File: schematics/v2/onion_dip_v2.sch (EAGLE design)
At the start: 38 parts, among them IC2 DS2432P

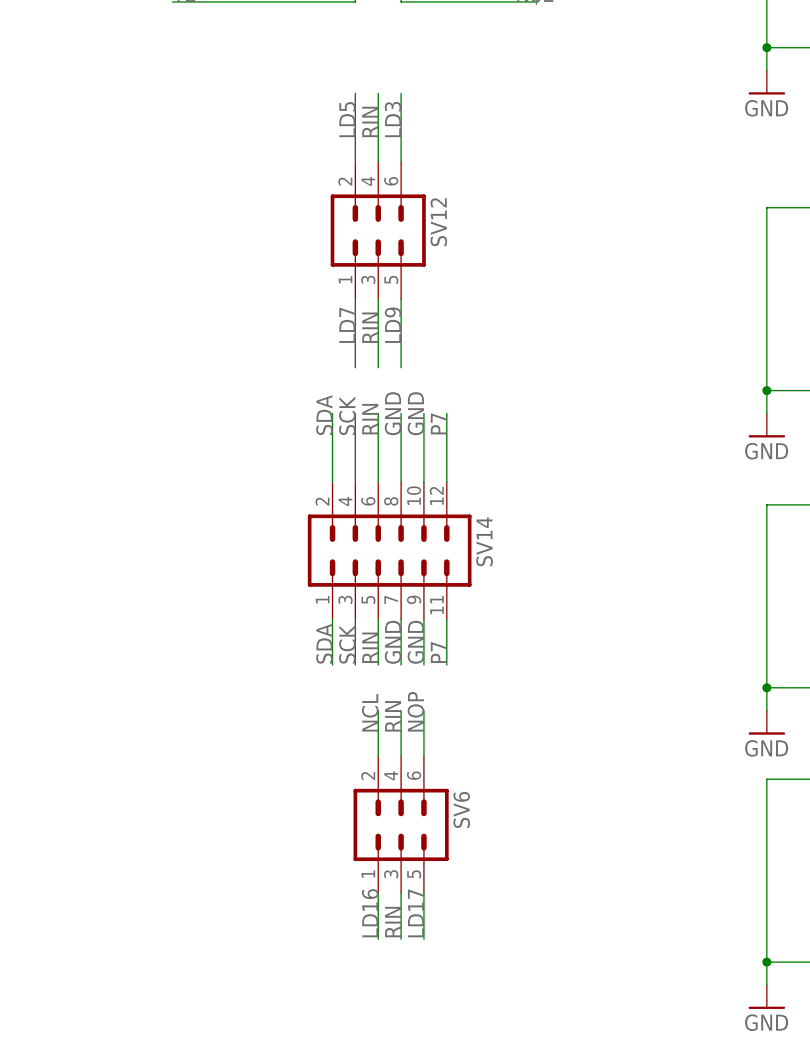
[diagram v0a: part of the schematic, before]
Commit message: increased isolation
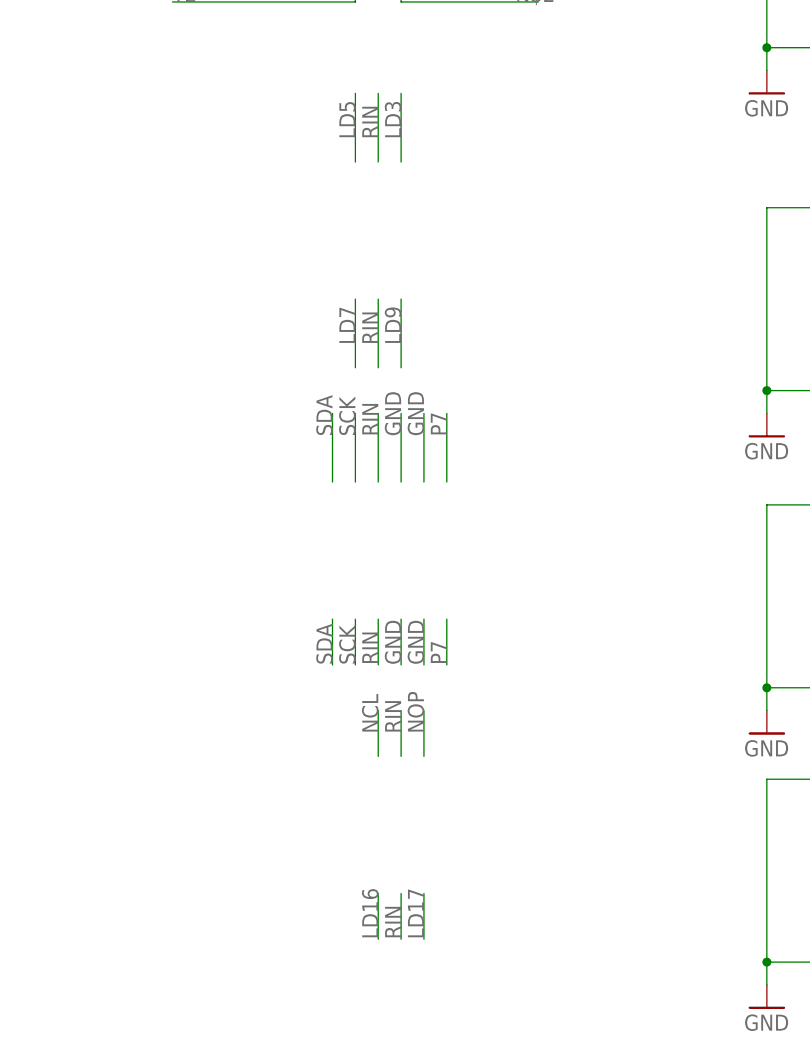
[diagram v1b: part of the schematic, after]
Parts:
- removed SV12, SV6: (no value), con-lstb_no_frame:MA03-2
- removed SV14: (no value), con-lstb_no_frame:MA06-2
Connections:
- net GND: no longer SV14.10, SV14.7, SV14.8, SV14.9
- net LD16: no longer SV6.1
- net LD17: no longer SV6.5
- net LD3: no longer SV12.6
- net LD5: no longer SV12.2
- net LD7: no longer SV12.1
- net LD9: no longer SV12.5
- net NCL: no longer SV6.2
- net NOP: no longer SV6.6
- net P7: no longer SV14.11, SV14.12
- net RIN: no longer SV12.3, SV12.4, SV14.5, SV14.6, SV6.3, SV6.4
- net SCK: no longer SV14.3, SV14.4
- net SDA: no longer SV14.1, SV14.2
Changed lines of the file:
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@@
 <part name="SV10" library="con-lstb_no_frame" deviceset="MA05-2" device=""/>
 <part name="SV11" library="con-lstb_no_frame" deviceset="MA05-2" device=""/>
-<part name="SV6" library="con-lstb_no_frame" deviceset="MA03-2" device=""/>
-<part name="SV12" library="con-lstb_no_frame" deviceset="MA03-2" device=""/>
-<part name="SV14" library="con-lstb_no_frame" deviceset="MA06-2" device=""/>
 <part name="SV20" library="con-lstb_no_frame" deviceset="MA07-2" device=""/>
 <part name="SV21" library="con-lstb_no_frame" deviceset="MA07-2" device=""/>
@@
 <instance part="SV10" gate="G$1" x="142.24" y="180.34" rot="R270"/>
 <instance part="SV11" gate="G$1" x="142.24" y="218.44" rot="R270"/>
-<instance part="SV6" gate="1" x="88.9" y="83.82" rot="R270"/>
-<instance part="SV12" gate="1" x="86.36" y="149.86" rot="R270"/>
-<instance part="SV14" gate="1" x="88.9" y="114.3" rot="R270"/>
 <instance part="SV20" gate="G$1" x="86.36" y="284.48" rot="R270"/>
 <instance part="SV21" gate="G$1" x="86.36" y="259.08" rot="R270"/>
@@
 </segment>
 <segment>
-<pinref part="SV14" gate="1" pin="2"/>
 <wire x1="81.28" y1="121.92" x2="81.28" y2="129.54" width="0.1524" layer="91"/>
 <label x="81.28" y="127" size="1.778" layer="95" rot="R90"/>
 </segment>
 <segment>
-<pinref part="SV14" gate="1" pin="1"/>
 <wire x1="81.28" y1="106.68" x2="81.28" y2="101.6" width="0.1524" layer="91"/>
 <label x="81.28" y="101.6" size="1.778" layer="95" rot="R90"/>
@@
 </segment>
 <segment>
-<pinref part="SV14" gate="1" pin="3"/>
 <wire x1="83.82" y1="106.68" x2="83.82" y2="101.6" width="0.1524" layer="91"/>
 <label x="83.82" y="101.6" size="1.778" layer="95" rot="R90"/>
 </segment>
 <segment>
-<pinref part="SV14" gate="1" pin="4"/>
 <wire x1="83.82" y1="121.92" x2="83.82" y2="129.54" width="0.1524" layer="91"/>
 <label x="83.82" y="127" size="1.778" layer="95" rot="R90"/>
@@
 </segment>
 <segment>
-<pinref part="SV14" gate="1" pin="8"/>
 <wire x1="88.9" y1="121.92" x2="88.9" y2="129.54" width="0.1524" layer="91"/>
 <label x="88.9" y="127" size="1.778" layer="95" rot="R90"/>
 </segment>
 <segment>
-<pinref part="SV14" gate="1" pin="10"/>
 <wire x1="91.44" y1="121.92" x2="91.44" y2="129.54" width="0.1524" layer="91"/>
 <label x="91.44" y="127" size="1.778" layer="95" rot="R90"/>
 </segment>
 <segment>
-<pinref part="SV14" gate="1" pin="7"/>
 <wire x1="88.9" y1="106.68" x2="88.9" y2="101.6" width="0.1524" layer="91"/>
 <label x="88.9" y="101.6" size="1.778" layer="95" rot="R90"/>
 </segment>
 <segment>
-<pinref part="SV14" gate="1" pin="9"/>
 <wire x1="91.44" y1="106.68" x2="91.44" y2="101.6" width="0.1524" layer="91"/>
 <label x="91.44" y="101.6" size="1.778" layer="95" rot="R90"/>
@@
 </segment>
 <segment>
-<pinref part="SV14" gate="1" pin="11"/>
 <wire x1="93.98" y1="106.68" x2="93.98" y2="101.6" width="0.1524" layer="91"/>
 <label x="93.98" y="101.6" size="1.778" layer="95" rot="R90"/>
 </segment>
 <segment>
-<pinref part="SV14" gate="1" pin="12"/>
 <wire x1="93.98" y1="121.92" x2="93.98" y2="129.54" width="0.1524" layer="91"/>
 <label x="93.98" y="127" size="1.778" layer="95" rot="R90"/>
@@
 </segment>
 <segment>
-<pinref part="SV6" gate="1" pin="1"/>
 <wire x1="86.36" y1="76.2" x2="86.36" y2="71.12" width="0.1524" layer="91"/>
 <label x="86.36" y="71.12" size="1.778" layer="95" rot="R90"/>
@@
 </segment>
 <segment>
-<pinref part="SV12" gate="1" pin="6"/>
 <wire x1="88.9" y1="157.48" x2="88.9" y2="165.1" width="0.1524" layer="91"/>
 <label x="88.9" y="160.02" size="1.778" layer="95" rot="R90"/>
@@
 </segment>
 <segment>
-<pinref part="SV12" gate="1" pin="2"/>
 <wire x1="83.82" y1="157.48" x2="83.82" y2="165.1" width="0.1524" layer="91"/>
 <label x="83.82" y="160.02" size="1.778" layer="95" rot="R90"/>
@@
 </segment>
 <segment>
-<pinref part="SV12" gate="1" pin="1"/>
 <wire x1="83.82" y1="142.24" x2="83.82" y2="134.62" width="0.1524" layer="91"/>
 <label x="83.82" y="137.16" size="1.778" layer="95" rot="R90"/>
@@
 </segment>
 <segment>
-<pinref part="SV12" gate="1" pin="5"/>
 <wire x1="88.9" y1="142.24" x2="88.9" y2="134.62" width="0.1524" layer="91"/>
 <label x="88.9" y="137.16" size="1.778" layer="95" rot="R90"/>
@@
 </segment>
 <segment>
-<pinref part="SV6" gate="1" pin="5"/>
 <wire x1="91.44" y1="76.2" x2="91.44" y2="71.12" width="0.1524" layer="91"/>
 <label x="91.44" y="71.12" size="1.778" layer="95" rot="R90"/>
@@
 </segment>
 <segment>
-<pinref part="SV12" gate="1" pin="3"/>
 <wire x1="86.36" y1="142.24" x2="86.36" y2="134.62" width="0.1524" layer="91"/>
 <label x="86.36" y="137.16" size="1.778" layer="95" rot="R90"/>
 </segment>
 <segment>
-<pinref part="SV14" gate="1" pin="6"/>
 <wire x1="86.36" y1="121.92" x2="86.36" y2="129.54" width="0.1524" layer="91"/>
 <label x="86.36" y="127" size="1.778" layer="95" rot="R90"/>
 </segment>
 <segment>
-<pinref part="SV14" gate="1" pin="5"/>
 <wire x1="86.36" y1="106.68" x2="86.36" y2="101.6" width="0.1524" layer="91"/>
 <label x="86.36" y="101.6" size="1.778" layer="95" rot="R90"/>
 </segment>
 <segment>
-<pinref part="SV6" gate="1" pin="4"/>
 <wire x1="88.9" y1="91.44" x2="88.9" y2="96.52" width="0.1524" layer="91"/>
 <label x="88.9" y="93.98" size="1.778" layer="95" rot="R90"/>
 </segment>
 <segment>
-<pinref part="SV6" gate="1" pin="3"/>
 <wire x1="88.9" y1="76.2" x2="88.9" y2="71.12" width="0.1524" layer="91"/>
 <label x="88.9" y="71.12" size="1.778" layer="95" rot="R90"/>
 </segment>
 <segment>
-<pinref part="SV12" gate="1" pin="4"/>
 <wire x1="86.36" y1="157.48" x2="86.36" y2="165.1" width="0.1524" layer="91"/>
 <label x="86.36" y="160.02" size="1.778" layer="95" rot="R90"/>
@@
 </segment>
 <segment>
-<pinref part="SV6" gate="1" pin="2"/>
 <wire x1="86.36" y1="91.44" x2="86.36" y2="96.52" width="0.1524" layer="91"/>
 <label x="86.36" y="93.98" size="1.778" layer="95" rot="R90"/>
@@
 </segment>
 <segment>
-<pinref part="SV6" gate="1" pin="6"/>
 <wire x1="91.44" y1="91.44" x2="91.44" y2="96.52" width="0.1524" layer="91"/>
 <label x="91.44" y="93.98" size="1.778" layer="95" rot="R90"/>

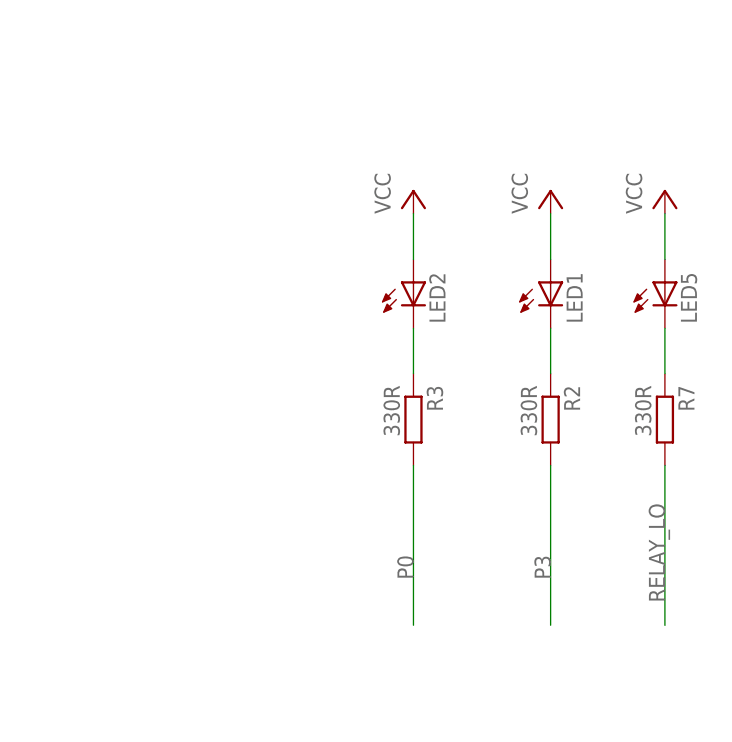
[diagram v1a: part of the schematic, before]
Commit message: changed led to 3.3V and reconnected LED1 to P1 (was P0)
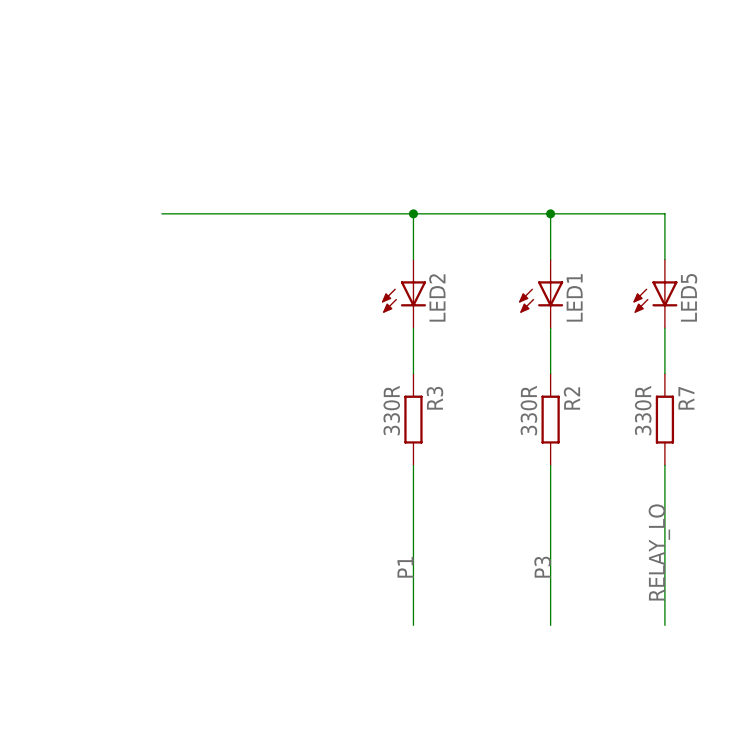
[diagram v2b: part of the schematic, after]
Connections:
- net P0: no longer R3.2
- net P1: now also R3.2
- net VCC: no longer LED1.A, LED2.A, LED5.A
- net _3V3: now also LED1.A, LED2.A, LED5.A
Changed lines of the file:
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@@
 <part name="SV20" library="con-lstb_no_frame" deviceset="MA07-2" device=""/>
 <part name="SV21" library="con-lstb_no_frame" deviceset="MA07-2" device=""/>
-<part name="P+2" library="supply1" deviceset="VCC" device=""/>
 <part name="P+4" library="supply1" deviceset="VCC" device=""/>
 <part name="P+6" library="supply1" deviceset="VCC" device=""/>
@@
 <part name="LED1" library="led" deviceset="LED" device="CHIP-LED0805"/>
 <part name="R2" library="rcl" deviceset="R-EU_" device="R0805" value="330R"/>
-<part name="P+5" library="supply1" deviceset="VCC" device=""/>
 <part name="LED2" library="led" deviceset="LED" device="CHIP-LED0805"/>
 <part name="R3" library="rcl" deviceset="R-EU_" device="R0805" value="330R"/>
-<part name="P+7" library="supply1" deviceset="VCC" device=""/>
 <part name="U$5" library="logo" deviceset="LOGO_10X10_SILK" device=""/>
 <part name="SV5" library="con-lstb_no_frame" deviceset="MA03-1" device=""/>
@@
 <instance part="SV20" gate="G$1" x="86.36" y="284.48" rot="R270"/>
 <instance part="SV21" gate="G$1" x="86.36" y="259.08" rot="R270"/>
-<instance part="P+2" gate="VCC" x="370.84" y="292.1"/>
 <instance part="P+4" gate="VCC" x="147.32" y="195.58" smashed="yes">
 <attribute name="VALUE" x="152.4" y="193.04" size="1.778" layer="96" rot="R90"/>
@@
 <instance part="LED1" gate="G$1" x="358.14" y="281.94"/>
 <instance part="R2" gate="G$1" x="358.14" y="266.7" rot="R270"/>
-<instance part="P+5" gate="VCC" x="358.14" y="292.1"/>
 <instance part="LED2" gate="G$1" x="342.9" y="281.94"/>
 <instance part="R3" gate="G$1" x="342.9" y="266.7" rot="R270"/>
-<instance part="P+7" gate="VCC" x="342.9" y="292.1"/>
 <instance part="U$5" gate="G$1" x="289.56" y="86.36"/>
 <instance part="SV5" gate="G$1" x="86.36" y="347.98" rot="R270"/>
@@
 <label x="157.48" y="88.9" size="1.778" layer="95"/>
 </segment>
+<segment>
+<pinref part="LED2" gate="G$1" pin="A"/>
+<wire x1="342.9" y1="284.48" x2="342.9" y2="289.56" width="0.1524" layer="91"/>
+<pinref part="LED5" gate="G$1" pin="A"/>
+<wire x1="370.84" y1="289.56" x2="370.84" y2="284.48" width="0.1524" layer="91"/>
+<wire x1="370.84" y1="289.56" x2="358.14" y2="289.56" width="0.1524" layer="91"/>
+<junction x="342.9" y="289.56"/>
+<wire x1="358.14" y1="289.56" x2="342.9" y2="289.56" width="0.1524" layer="91"/>
+<wire x1="342.9" y1="289.56" x2="314.96" y2="289.56" width="0.1524" layer="91"/>
+<pinref part="LED1" gate="G$1" pin="A"/>
+<wire x1="358.14" y1="289.56" x2="358.14" y2="284.48" width="0.1524" layer="91"/>
+<junction x="358.14" y="289.56"/>
+</segment>
 </net>
 <net name="_1V8" class="0">
@@
 <label x="142.24" y="203.2" size="1.778" layer="95" rot="R90"/>
 </segment>
+<segment>
+<pinref part="R3" gate="G$1" pin="2"/>
+<wire x1="342.9" y1="261.62" x2="342.9" y2="243.84" width="0.1524" layer="91"/>
+<label x="342.9" y="248.92" size="1.778" layer="95" rot="R90"/>
+</segment>
 </net>
 <net name="AP" class="0">
@@
 <wire x1="139.7" y1="210.82" x2="139.7" y2="200.66" width="0.1524" layer="91"/>
 <label x="139.7" y="203.2" size="1.778" layer="95" rot="R90"/>
-</segment>
-<segment>
-<pinref part="R3" gate="G$1" pin="2"/>
-<wire x1="342.9" y1="261.62" x2="342.9" y2="243.84" width="0.1524" layer="91"/>
-<label x="342.9" y="248.92" size="1.778" layer="95" rot="R90"/>
 </segment>
 </net>
@@
 </segment>
 <segment>
-<pinref part="LED5" gate="G$1" pin="A"/>
-<wire x1="370.84" y1="289.56" x2="370.84" y2="284.48" width="0.1524" layer="91"/>
-<pinref part="P+2" gate="VCC" pin="VCC"/>
-</segment>
-<segment>
 <pinref part="SV10" gate="G$1" pin="10"/>
 <pinref part="P+4" gate="VCC" pin="VCC"/>
@@
 </segment>
 <segment>
-<pinref part="LED1" gate="G$1" pin="A"/>
-<pinref part="P+5" gate="VCC" pin="VCC"/>
-<wire x1="358.14" y1="289.56" x2="358.14" y2="284.48" width="0.1524" layer="91"/>
-</segment>
-<segment>
-<pinref part="P+7" gate="VCC" pin="VCC"/>
-<pinref part="LED2" gate="G$1" pin="A"/>
-<wire x1="342.9" y1="284.48" x2="342.9" y2="289.56" width="0.1524" layer="91"/>
-</segment>
-<segment>

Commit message: v2, clearance on relay; leds; usb jack; pulldowns
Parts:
- removed ASDASD: (no value), pinhead:PINHD-1X6
- removed D1: BAS70, diode:BAS70
- removed JP3: (no value), jumper:JP2E
- removed SV1, SV4, SV9: (no value), con-lstb_no_frame:MA05-2
- removed SV5, SV8: (no value), con-lstb_no_frame:MA03-1
- added COMM: (no value), pinhead:PINHD-1X6
- added I2C_1, SPI2_1, SPI2_2: (no value), con-lstb_no_frame:MA05-2
- added PWRCH: (no value), jumper:SJ2W
- added R4, R5, R6: 10k, rcl:R-EU_R0805
- added USB: USBUSB-MICROB-SMT-DIP, Spark:USBUSB-MICROB-SMT-DIP
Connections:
- removed net N$2: SV8.2, SV8.3
- net 3V3: no longer SV5.2
- net CHIP_5V: now also PWRCH.1; no longer JP3.1
- net CHR_IN: now also PWRCH.3; no longer JP3.3
- net CSICK: now also SPI2_1.6, SPI2_2.6; no longer SV4.6, SV9.6
- net CSIHSYNC: now also SPI2_1.3, SPI2_2.3; no longer SV4.3, SV9.3
- net CSIPCK: now also SPI2_1.4, SPI2_2.4; no longer SV4.4, SV9.4
- net CSVSYNC: now also SPI2_1.5, SPI2_2.5; no longer SV4.5, SV9.5
- net D2: now also SPI2_2.7; no longer SV4.7
- net D3: now also SPI2_2.8; no longer SV4.8
- net GND: now also COMM.1, I2C_1.1, I2C_1.2, SPI2_1.1, SPI2_1.2, SPI2_2.1, SPI2_2.2, USB.GND; no longer ASDASD.1, SV1.1, SV1.2, SV4.1, SV4.2, SV5.1, SV9.1, SV9.2
- net N$29: now also R6.2
- net N$3: now also R5.2
- net N$30: now also I2C_1.8; no longer SV1.8
- net N$35: now also I2C_1.7; no longer SV1.7
- net N$4: now also R4.2
- net N4: now also SPI2_1.7, SPI2_1.8; no longer SV9.7, SV9.8
- net N5: now also SPI2_1.10, SPI2_1.9; no longer SV9.10, SV9.9
- net RELAY_LO: now also U$1.COIL1; no longer D1.A, U$1.COIL0
- net RX: now also COMM.4; no longer ASDASD.4
- net SCL2: now also I2C_1.5, I2C_1.6; no longer SV1.5, SV1.6
- net SDA2: now also I2C_1.3, I2C_1.4; no longer SV1.3, SV1.4
- net TX: now also COMM.5; no longer ASDASD.5
- net VCC: now also PWRCH.2, SPI2_2.10, SPI2_2.9, U$1.COIL0, USB.VBUS; no longer D1.C, JP3.2, SV4.10, SV4.9, SV5.3, U$1.COIL1
- net Y2: no longer SV8.1
- net _3V3: now also I2C_1.10, I2C_1.9, R4.1, R5.1, R6.1; no longer SV1.10, SV1.9
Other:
- note added: "Connectors"
- note added: "EEPROM"
- note added: "LED"
- note added: "Power"
- note added: "Relay"
- moved on the sheet: D2, GND, IC2, IC2P, IC2_1W, IN, LED1, LED2, LED5, N_CLOSE, N_OPEN, R1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
